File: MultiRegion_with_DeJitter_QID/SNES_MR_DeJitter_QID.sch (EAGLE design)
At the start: 80 parts, among them J1 SNESCART_CONN_SPARSE_4, Q31 2SC2412, U1 SuperCIC_lock, U2 uIGR, U3 EPM7032AETC44-10N, U4 74HCT2G125DP, U5 CDCE913, U6 2G17TI_DBV, U7 TLV70033, U8 TLV70018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

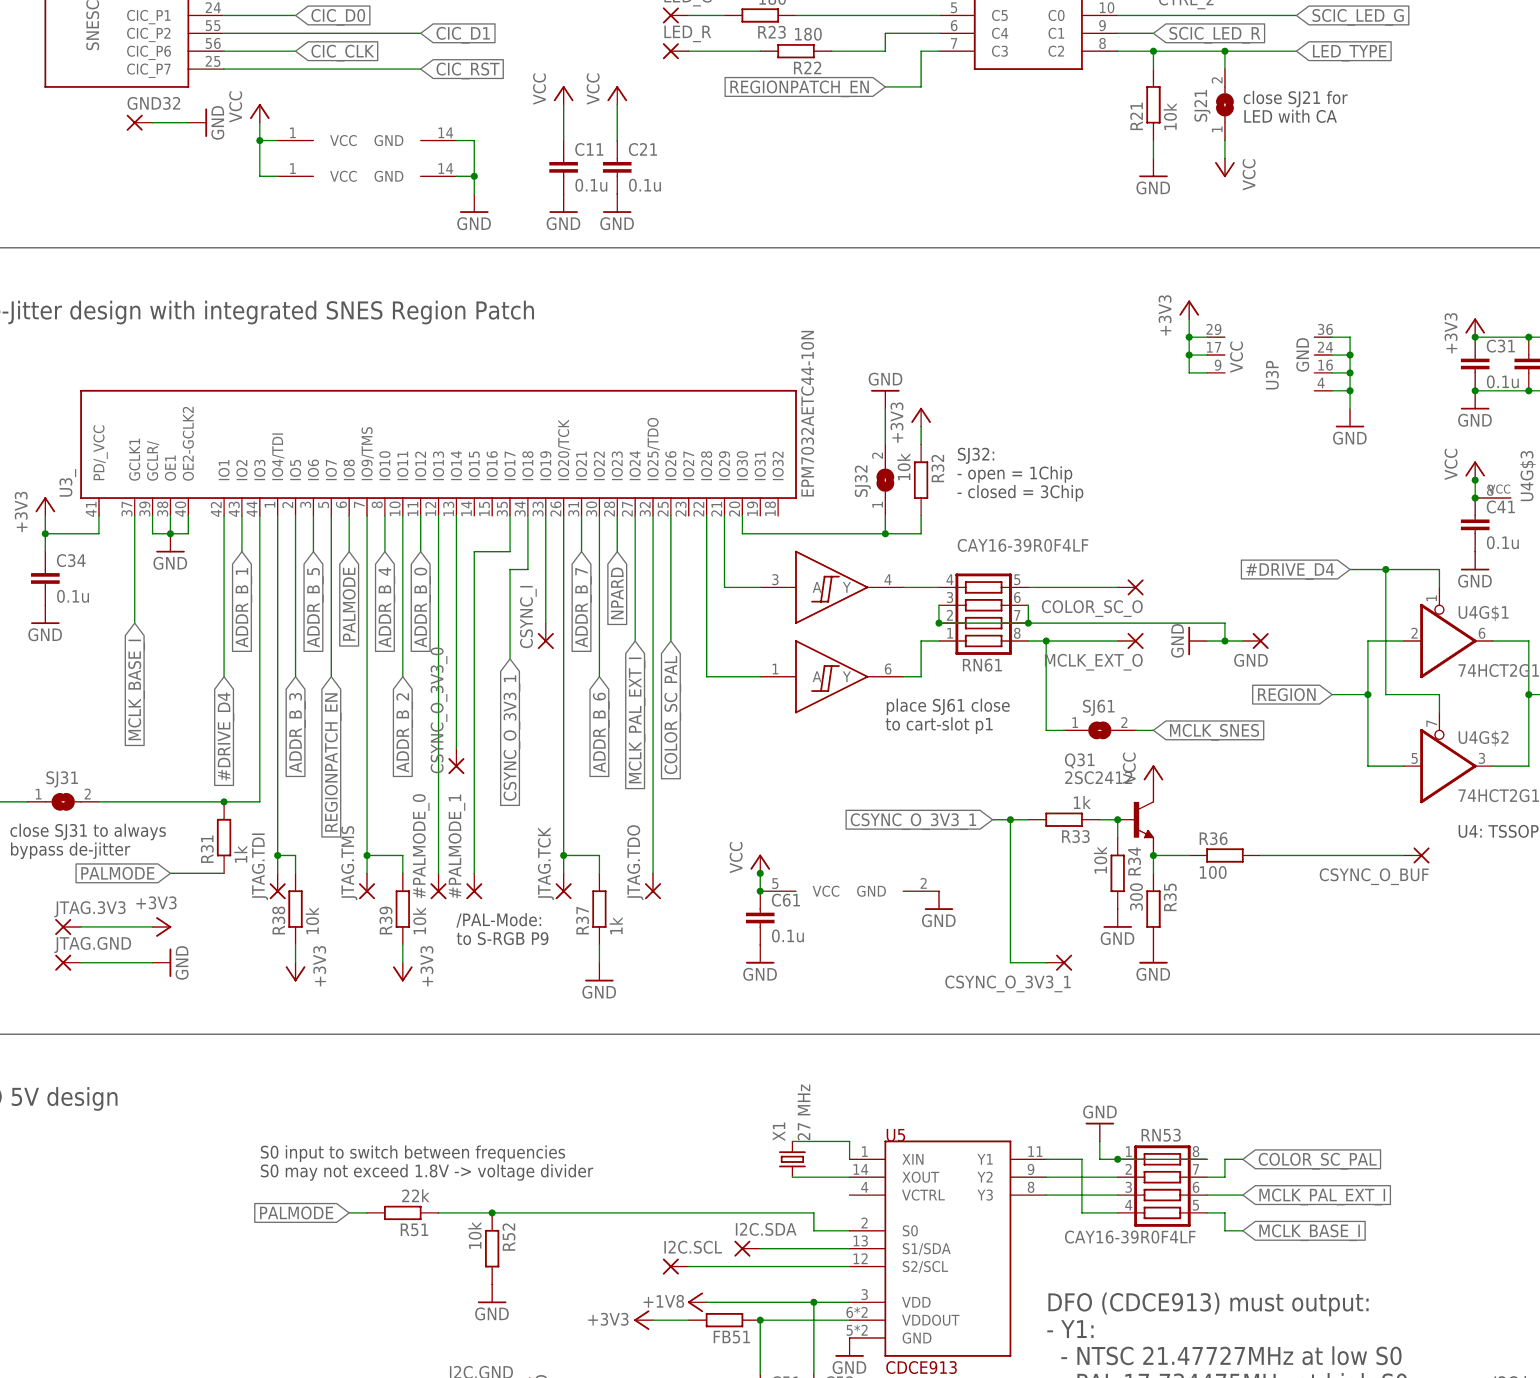
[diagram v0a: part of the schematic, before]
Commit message: PCB update: - double /CS.i pad - color carrier generate inside CPLD (trace removed) - replace resistor arrays by simple components - add footprint for resistor from SNES mainboard to have resistor not loosely connected
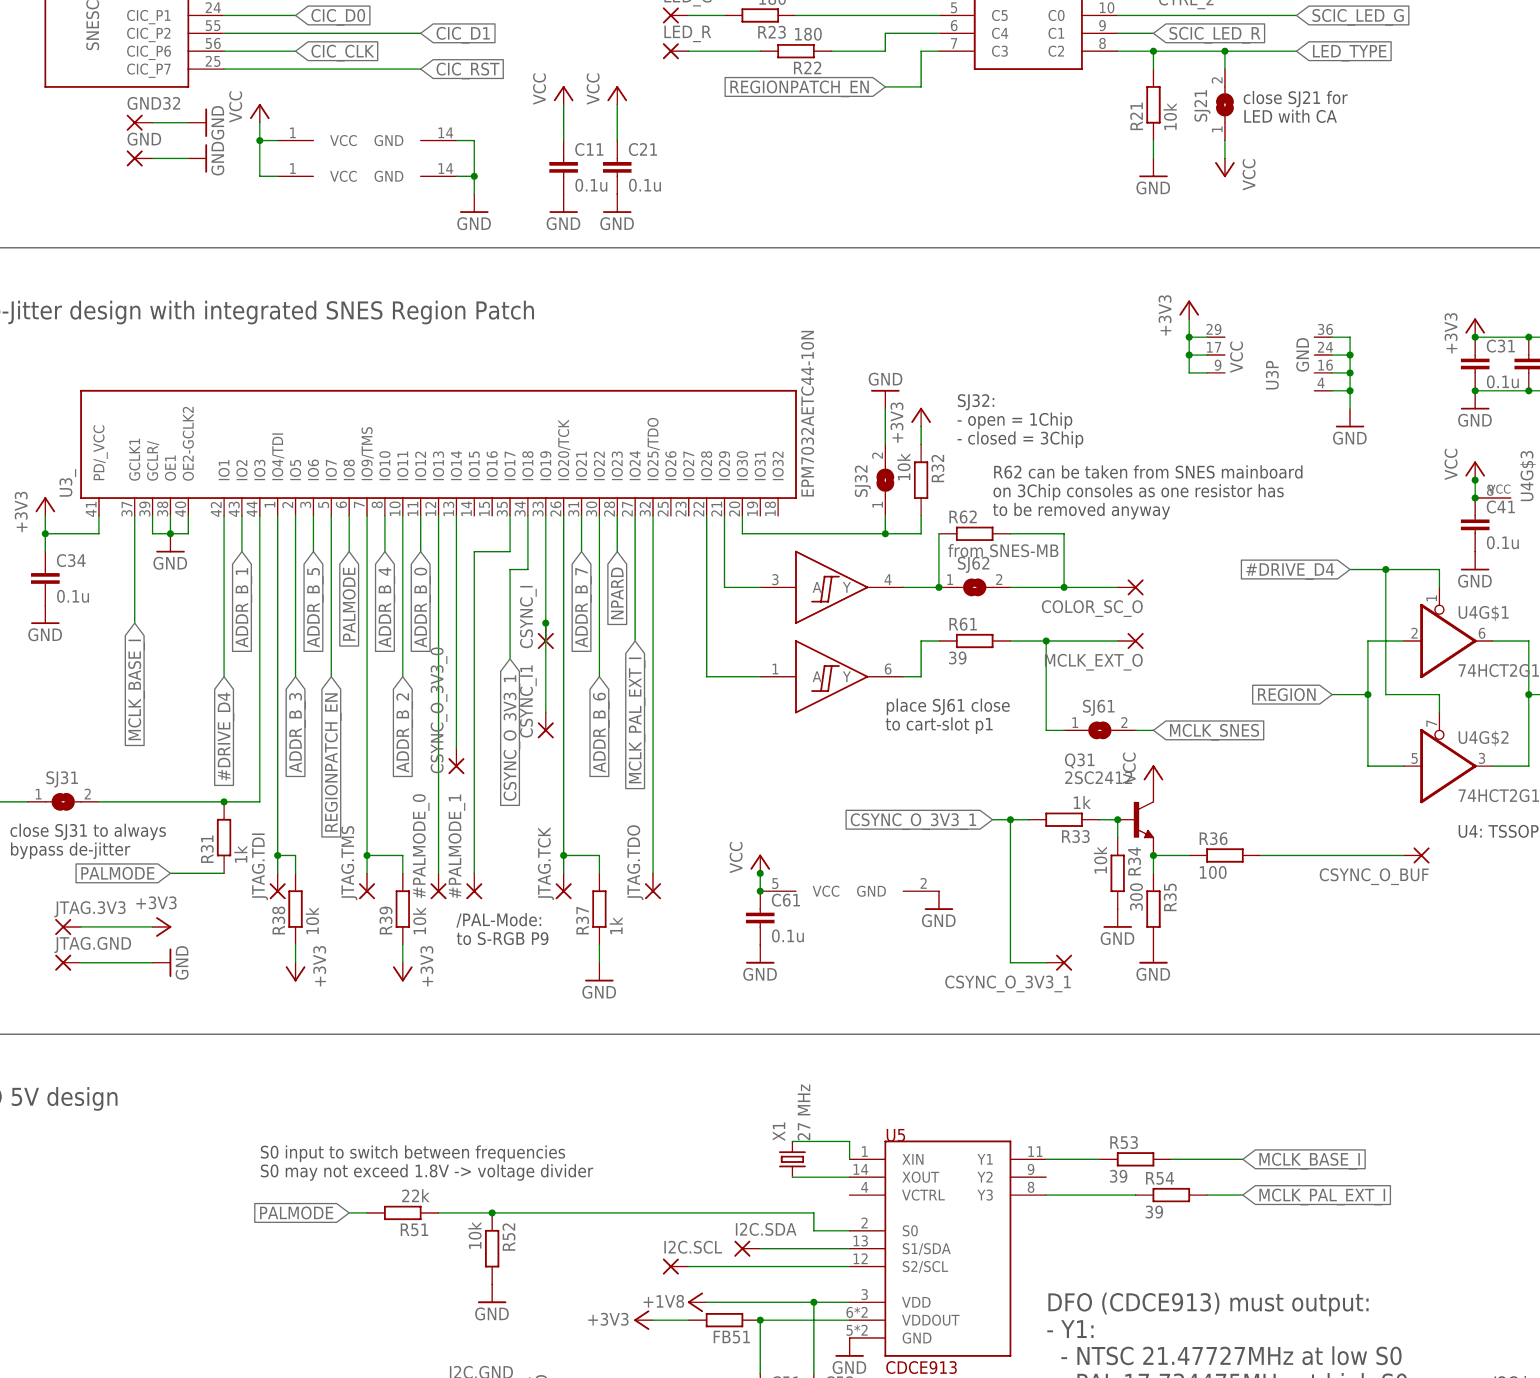
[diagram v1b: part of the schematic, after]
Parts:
- removed RN53, RN61: CAY16-39R0F4LF, resistor-net:CTS742C083
- added CSYNC_I1: (no value), wirepad:SMD2
- added R53, R54, R61: 39, rcl:R-EU_R0603
- added R62: from SNES-MB, rcl:R-EU_R0805
- added SJ62: (no value), jumper:SJSMALL
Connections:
- removed net COLOR_SC_NTSC_PRE: RN53.3, U5.Y3
- removed net COLOR_SC_PAL: RN53.7, U3_.IO26
- removed net COLOR_SC_PAL_PRE: RN53.2, U5.Y2
- new net MCLK_PAL_EXT_I_PRE: R54.1, U5.Y3
- net COLOR_SC_O: now also R62.2, SJ62.2; no longer RN61.5
- net COLOR_SC_O_PRE: now also R62.1, SJ62.1; no longer RN61.4
- net CSYNC_I: now also CSYNC_I1.P
- net GND: no longer RN53.1, RN53.8, RN61.2, RN61.3, RN61.6, RN61.7
- net MCLK_BASE_I: now also R53.2; no longer RN53.5
- net MCLK_BASE_I_PRE: now also R53.1; no longer RN53.4
- net MCLK_EXT_O: now also R61.2; no longer RN61.8
- net MCLK_EXT_O_PRE: now also R61.1; no longer RN61.1
- net MCLK_PAL_EXT_I: now also R54.2; no longer RN53.6
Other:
- note added: "R62 can be taken from SNES mainboard on 3Chip consoles as one resistor has to be removed anyway"
- moved on the sheet: GND

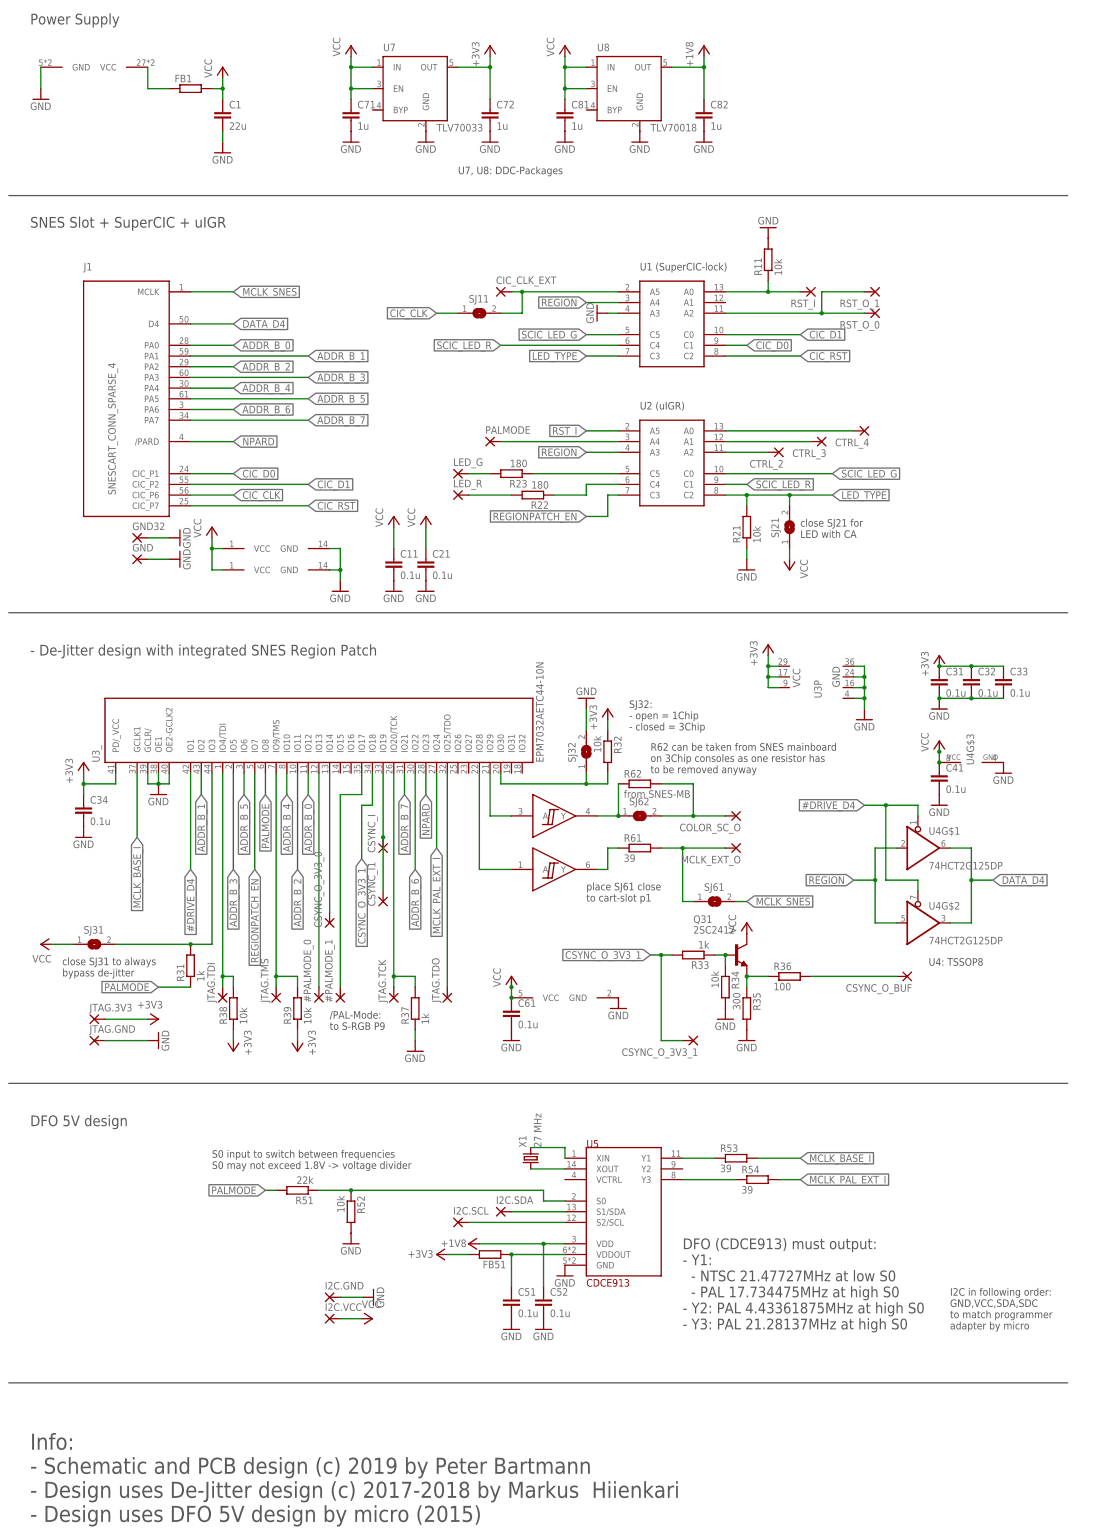
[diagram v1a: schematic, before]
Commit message: update PCB design: - selectable sync level for the buffered output - video buffer for sync instead of transistor - color carrier fix applied - some GND between sub-carrier and master clock output
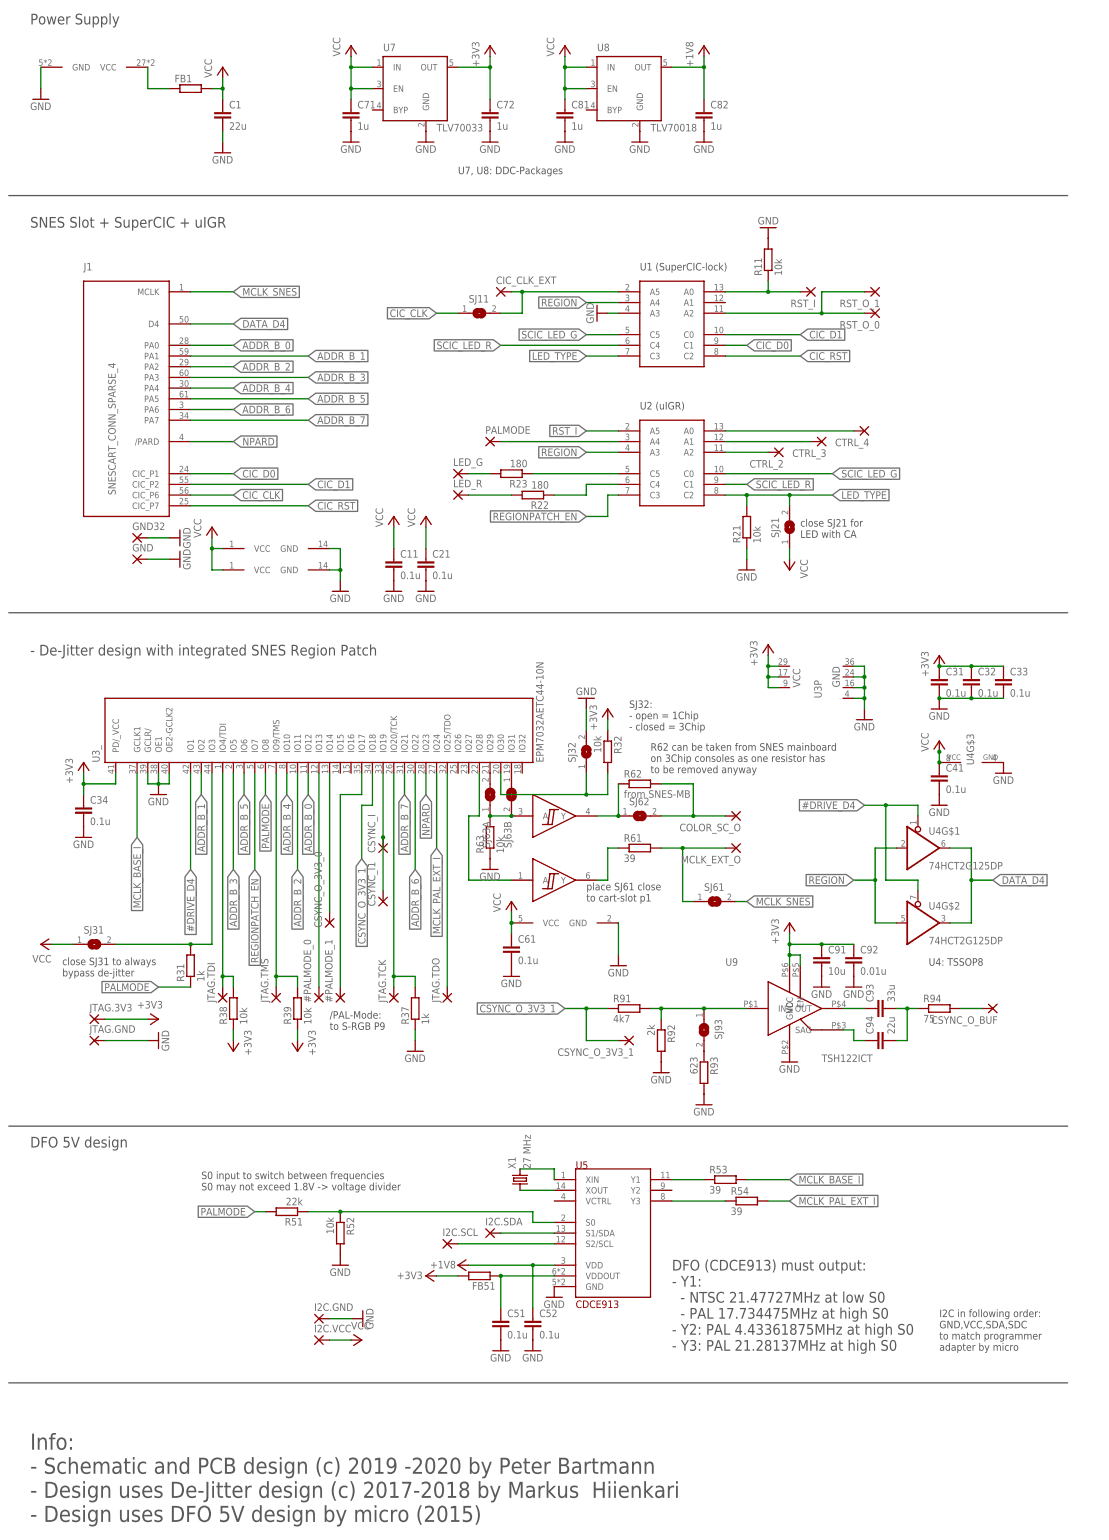
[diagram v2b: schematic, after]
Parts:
- removed Q31: 2SC2412, transistor:MMBTH24LT1-NPN-SOT23-BEC
- removed R33: 1k, rcl:R-EU_R0603
- removed R34: 10k, rcl:R-EU_R0603
- removed R35: 300, rcl:R-EU_R0603
- removed R36: 100, rcl:R-EU_R0603
- added C91: 10u, rcl:C-EUC0603
- added C92: 0.01u, rcl:C-EUC0603
- added C93: 33u, rcl:C-EUC0805
- added C94: 22u, rcl:C-EUC0603
- added R63: 10k, rcl:R-EU_R0805
- added R91: 4k7, rcl:R-EU_R0603
- added R92: 2k, rcl:R-EU_R0603
- added R93: 623, rcl:R-EU_R0603
- added R94: 75, rcl:R-EU_R0603
- added SJ63A, SJ63B, SJ93: (no value), jumper:SJSMALL
- added U9: TSH122ICT, st-microelectronics:TSH122ICT
- C1: device rcl:C-EUC0805 -> rcl:C-EUC0603
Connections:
- net COLOR_SC_O renamed COLOR_SC_PCB_O
- removed net CSYNC_O_POST_Q: Q31.E, R35.1, R36.1
- removed net CSYNC_O_PRE_Q: Q31.B, R33.1, R34.1
- new net COLOR_SC_OPT_O_PRE: SJ63B.1, U3_.IO31
- new net COLOR_SC_PCB_O_PRE: R62.1, SJ62.1, U6G$2.Y
- new net N$1: R91.2, R92.1, SJ93.1, U9.IN
- new net N$10: R93.1, SJ93.2
- new net N$7: C94.1, U9.SAG
- new net N$8: C93.1, U9.OUT
- new net N$9: C93.2, C94.2, R94.1
- net +3V3: now also C91.1, C92.1, U9.EN, U9.VCC
- net +5V: no longer Q31.C
- net COLOR_SC_O_PRE: now also SJ63A.2, U3_.IO29; no longer R62.1, SJ62.1, U6G$2.Y
- net COLOR_SC_PRE: now also R63.2, SJ63A.1, SJ63B.2; no longer U3_.IO29
- net CSYNC_O: now also R94.2; no longer R36.2
- net CSYNC_O_3V3_1: now also R91.1; no longer R33.2
- net GND: now also C91.2, C92.2, R63.1, R92.2, R93.2, U9.GND; no longer R34.2, R35.2
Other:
- note added: "Info: - Schematic and PCB design (c) 2019 -2020 by Peter Bartmann - Design uses De-Jitter design (c) 2017-2018 by Markus Hiienkari - Design uses DFO 5V design by micro (2015)"
- note removed: "Info: - Schematic and PCB design (c) 2019 by Peter Bartmann - Design uses De-Jitter design (c) 2017-2018 by Markus Hiienkari - Design uses DFO 5V design by micro (2015)"
- moved on the sheet: C51, C52, C61, CSYNC_O_3V3_1, CSYNC_O_BUF, FB51, I2C.GND, I2C.SCL, I2C.SDA, I2C.VCC, R51, R52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
